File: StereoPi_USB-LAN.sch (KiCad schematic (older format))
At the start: 58 parts, among them T1 Pulse_J0011D01BNL, Y1 25MHz

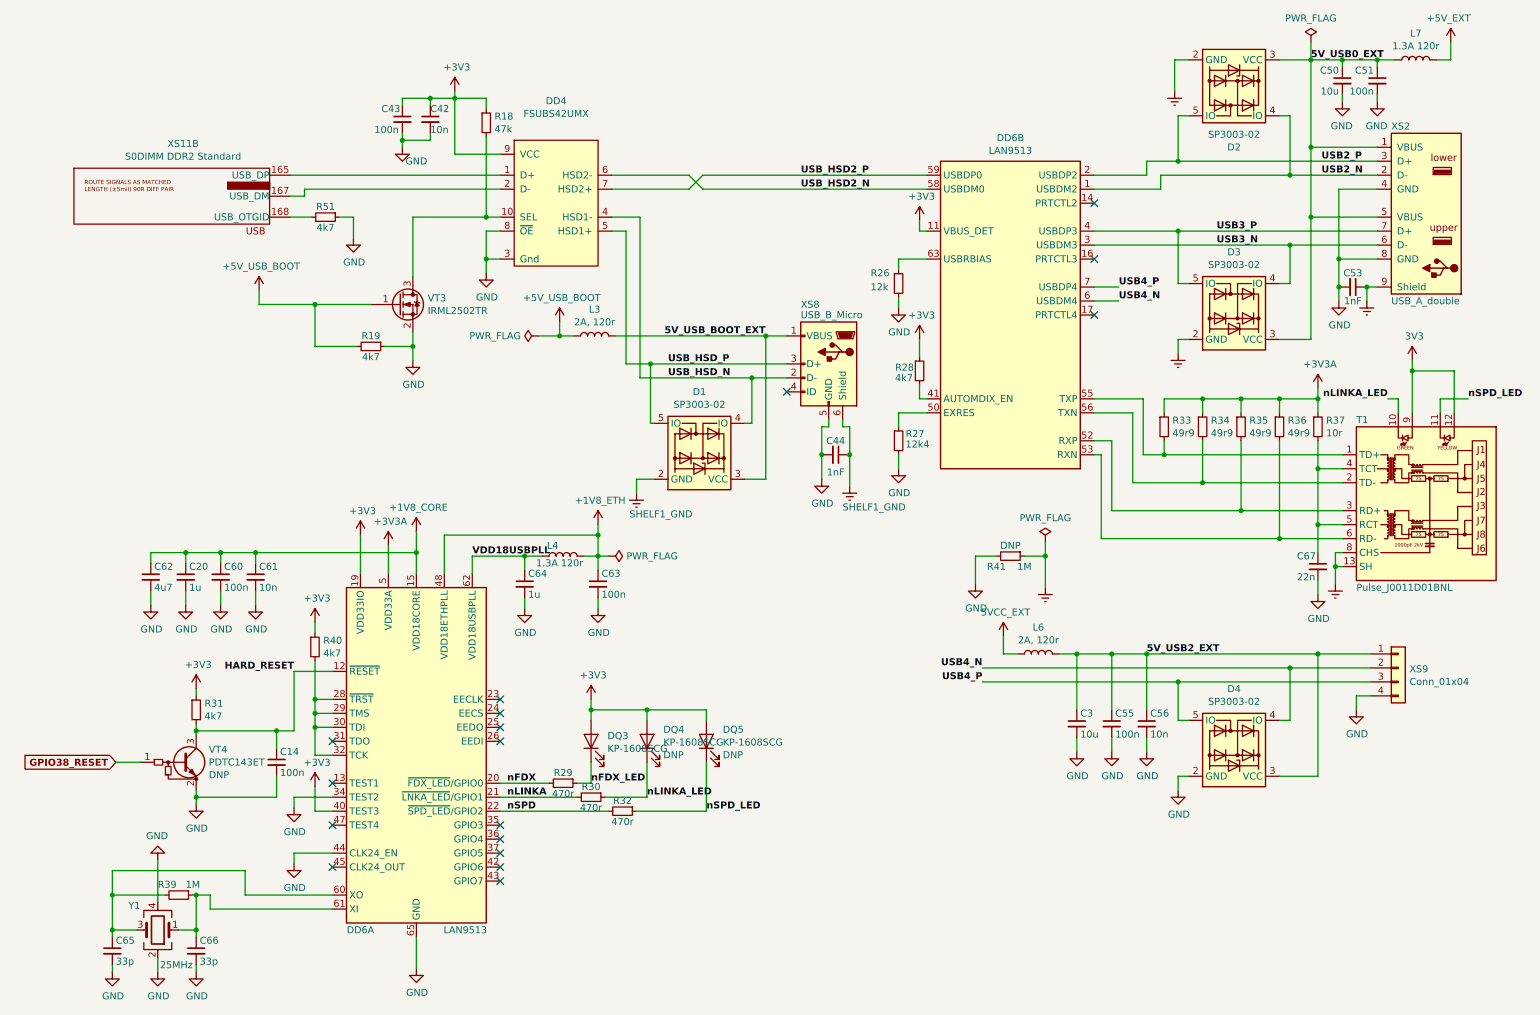
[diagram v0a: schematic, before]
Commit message: added Voltages to Caps, reformatted labels
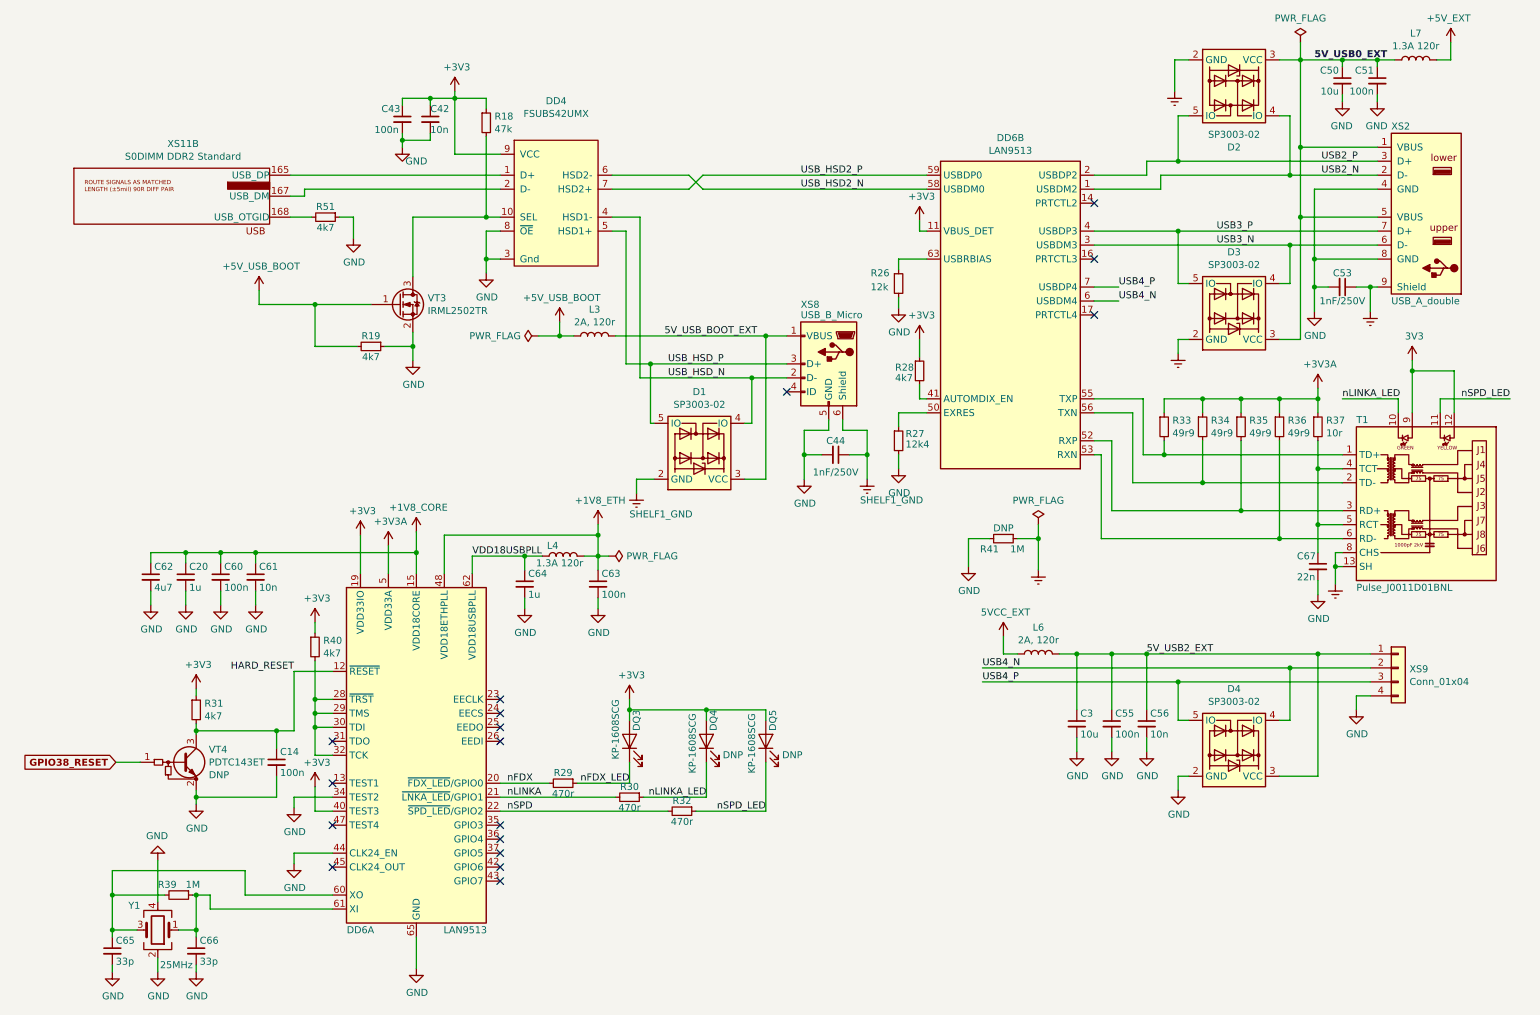
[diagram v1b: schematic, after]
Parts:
- C44, C53: value 1nF -> 1nF/250V
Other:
- moved on the sheet: C53, DQ3, DQ4, DQ5, R30, R32, R41
